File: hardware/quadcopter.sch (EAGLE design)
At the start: 66 parts, among them J1 AVR_SPI_PRG_6NS, J2 HEADER-4POS-2X2-0.1IN-FEMALE-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, J3 HEADER-10POSTH-254X10, J4 HEADER-4POS-2X2-0.1IN-FEMALE-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, Q3 MOSFET-FET-SI2302CDS-T1-E3CT-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, Q4 MOSFET-FET-SI2302CDS-T1-E3CT-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, Q5 MOSFET-FET-SI2302CDS-T1-E3CT-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, Q6 MOSFET-FET-SI2302CDS-T1-E3CT-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, U1 ATMEGA128RFA1, U2 IMU-LSM6DSOXTR-497-18367-1-ND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, Y1 CRYSTAL5X3

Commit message: please work
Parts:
- removed D10, D3, D4, D9: (no value), custom_v9:LED-RED-160-1178-1-ND
- added U$1, U$4, U$5, U$6: LED_BLUE, LED:LED_BLUE
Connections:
- removed net N$12: C9.2, U2.VDD
- net 3V: now also C9.2, U2.VDD
- net LED1: no longer D3.A
- net LED2: no longer D4.A
- net LED3: no longer D9.A
- net LED4: no longer D10.A
- net N$22: no longer D10.C, D3.C, D4.C, D9.C
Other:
- moved on the sheet: R6
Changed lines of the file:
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@@
 <part name="J3" library="quadparts_prebuilt_2022" deviceset="HEADER-10POS" device="TH-254X10"/>
 <part name="J4" library="quadparts_prebuilt_2022" deviceset="HEADER-4POS" device="-2X2-0.1IN-FEMALE-SMD-BOTTOM-ENTRY"/>
-<part name="D3" library="custom_v9" deviceset="LED" device="-RED-160-1178-1-ND"/>
-<part name="D4" library="custom_v9" deviceset="LED" device="-RED-160-1178-1-ND"/>
-<part name="D9" library="custom_v9" deviceset="LED" device="-RED-160-1178-1-ND"/>
-<part name="D10" library="custom_v9" deviceset="LED" device="-RED-160-1178-1-ND"/>
 <part name="GND23" library="quadparts_prebuilt_2022" deviceset="GND" device=""/>
 <part name="R6" library="quadparts_prebuilt_2022" deviceset="RESISTOR_" device="SMD-2012-0805-604" value="604"/>
@@
 <part name="GND43" library="quadparts_prebuilt_2022" deviceset="GND" device=""/>
 <part name="P+19" library="quadparts_prebuilt_2022" deviceset="3V" device=""/>
+<part name="U$1" library="LED" library_urn="urn:adsk.wipprod:fs.file:vf.dgQ34RYLRkWtLog4lTO-XQ" deviceset="LED_BLUE" device=""/>
+<part name="U$4" library="LED" library_urn="urn:adsk.wipprod:fs.file:vf.dgQ34RYLRkWtLog4lTO-XQ" deviceset="LED_BLUE" device=""/>
+<part name="U$5" library="LED" library_urn="urn:adsk.wipprod:fs.file:vf.dgQ34RYLRkWtLog4lTO-XQ" deviceset="LED_BLUE" device=""/>
+<part name="U$6" library="LED" library_urn="urn:adsk.wipprod:fs.file:vf.dgQ34RYLRkWtLog4lTO-XQ" deviceset="LED_BLUE" device=""/>
 </parts>
 <sheets>
@@
 <attribute name="NAME" x="155.702" y="55.88" size="1.778" layer="95" rot="R180"/>
 </instance>
-<instance part="D3" gate="G$1" x="91.44" y="7.62" smashed="yes">
-<attribute name="NAME" x="86.36" y="10.16" size="1.778" layer="95"/>
-<attribute name="VALUE" x="86.36" y="2.54" size="1.778" layer="96"/>
-</instance>
-<instance part="D4" gate="G$1" x="91.44" y="0" smashed="yes">
-<attribute name="NAME" x="86.36" y="2.54" size="1.778" layer="95"/>
-<attribute name="VALUE" x="86.36" y="-5.08" size="1.778" layer="96"/>
-</instance>
-<instance part="D9" gate="G$1" x="91.44" y="-7.62" smashed="yes">
-<attribute name="NAME" x="86.36" y="-5.08" size="1.778" layer="95"/>
-<attribute name="VALUE" x="86.36" y="-12.7" size="1.778" layer="96"/>
-</instance>
-<instance part="D10" gate="G$1" x="91.44" y="-15.24" smashed="yes">
-<attribute name="NAME" x="86.36" y="-12.7" size="1.778" layer="95"/>
-<attribute name="VALUE" x="86.36" y="-20.32" size="1.778" layer="96"/>
-</instance>
-<instance part="GND23" gate="1" x="96.52" y="-43.18" smashed="yes">
-<attribute name="VALUE" x="96.52" y="-45.72" size="1.778" layer="96" align="center"/>
-</instance>
-<instance part="R6" gate="G$1" x="96.52" y="-27.94" smashed="yes" rot="R90">
-<attribute name="VALUE" x="99.822" y="-31.75" size="1.778" layer="96" rot="R90"/>
-<attribute name="NAME" x="95.0214" y="-31.75" size="1.778" layer="95" rot="R90"/>
+<instance part="GND23" gate="1" x="104.14" y="-43.18" smashed="yes">
+<attribute name="VALUE" x="104.14" y="-45.72" size="1.778" layer="96" align="center"/>
+</instance>
+<instance part="R6" gate="G$1" x="104.14" y="-27.94" smashed="yes" rot="R90">
+<attribute name="VALUE" x="107.442" y="-31.75" size="1.778" layer="96" rot="R90"/>
+<attribute name="NAME" x="102.6414" y="-31.75" size="1.778" layer="95" rot="R90"/>
 </instance>
 <instance part="GND37" gate="1" x="121.92" y="-43.18" smashed="yes">
@@
 <attribute name="VALUE" x="83.82" y="-91.44" size="1.778" layer="96" rot="R180" align="center"/>
 </instance>
+<instance part="U$1" gate="G$1" x="93.98" y="0" smashed="yes"/>
+<instance part="U$4" gate="G$1" x="93.98" y="7.62" smashed="yes"/>
+<instance part="U$5" gate="G$1" x="93.98" y="-15.24" smashed="yes"/>
+<instance part="U$6" gate="G$1" x="93.98" y="-7.62" smashed="yes"/>
 </instances>
 <busses>
@@
 </segment>
 <segment>
-<wire x1="96.52" y1="-33.02" x2="96.52" y2="-40.64" width="0.1524" layer="91"/>
+<wire x1="104.14" y1="-33.02" x2="104.14" y2="-40.64" width="0.1524" layer="91"/>
 <pinref part="GND23" gate="1" pin="GND"/>
 <pinref part="R6" gate="G$1" pin="1"/>
@@
 <junction x="68.58" y="-101.6"/>
 </segment>
+<segment>
+<pinref part="P+6" gate="G$1" pin="3V"/>
+<wire x1="119.38" y1="134.62" x2="119.38" y2="127" width="0.1524" layer="91"/>
+<pinref part="U2" gate="G$1" pin="VDD"/>
+<wire x1="124.46" y1="127" x2="119.38" y2="127" width="0.1524" layer="91"/>
+<pinref part="C9" gate="G$1" pin="2"/>
+<junction x="119.38" y="127"/>
+</segment>
 </net>
 <net name="SCK" class="0">
@@
 </segment>
 <segment>
-<pinref part="D4" gate="G$1" pin="A"/>
 <wire x1="86.36" y1="0" x2="81.28" y2="0" width="0.1524" layer="91"/>
 <label x="81.28" y="0" size="1.778" layer="95" rot="R180" xref="yes"/>
@@
 </segment>
 <segment>
-<pinref part="D9" gate="G$1" pin="A"/>
 <wire x1="86.36" y1="-7.62" x2="81.28" y2="-7.62" width="0.1524" layer="91"/>
 <label x="81.28" y="-7.62" size="1.778" layer="95" rot="R180" xref="yes"/>
@@
 </segment>
 <segment>
-<pinref part="D10" gate="G$1" pin="A"/>
 <wire x1="86.36" y1="-15.24" x2="81.28" y2="-15.24" width="0.1524" layer="91"/>
 <label x="81.28" y="-15.24" size="1.778" layer="95" rot="R180" xref="yes"/>
@@
 <pinref part="J2" gate="G$1" pin="1"/>
 <pinref part="C13" gate="G$1" pin="2"/>
-</segment>
-</net>
-<net name="N$12" class="0">
-<segment>
-<pinref part="U2" gate="G$1" pin="VDD"/>
-<wire x1="124.46" y1="127" x2="119.38" y2="127" width="0.1524" layer="91"/>
-<wire x1="119.38" y1="134.62" x2="119.38" y2="127" width="0.1524" layer="91"/>
-<pinref part="P+6" gate="G$1" pin="3V"/>
-<pinref part="C9" gate="G$1" pin="2"/>
-<junction x="119.38" y="127"/>
 </segment>
 </net>
@@
 </segment>
 <segment>
-<pinref part="D3" gate="G$1" pin="A"/>
 <wire x1="86.36" y1="7.62" x2="81.28" y2="7.62" width="0.1524" layer="91"/>
 <label x="81.28" y="7.62" size="1.778" layer="95" rot="R180" xref="yes"/>
@@
 <net name="N$22" class="0">
 <segment>
-<pinref part="D3" gate="G$1" pin="C"/>
-<pinref part="D4" gate="G$1" pin="C"/>
-<wire x1="96.52" y1="-15.24" x2="96.52" y2="-7.62" width="0.1524" layer="91"/>
-<wire x1="96.52" y1="-7.62" x2="96.52" y2="0" width="0.1524" layer="91"/>
-<wire x1="96.52" y1="0" x2="96.52" y2="7.62" width="0.1524" layer="91"/>
-<pinref part="D9" gate="G$1" pin="C"/>
-<pinref part="D10" gate="G$1" pin="C"/>
-<junction x="96.52" y="0"/>
-<junction x="96.52" y="-7.62"/>
-<wire x1="96.52" y1="-15.24" x2="96.52" y2="-22.86" width="0.1524" layer="91"/>
-<junction x="96.52" y="-15.24"/>
+<wire x1="104.14" y1="-15.24" x2="104.14" y2="-7.62" width="0.1524" layer="91"/>
+<wire x1="104.14" y1="-7.62" x2="104.14" y2="0" width="0.1524" layer="91"/>
+<wire x1="104.14" y1="0" x2="104.14" y2="7.62" width="0.1524" layer="91"/>
+<wire x1="104.14" y1="-15.24" x2="104.14" y2="-22.86" width="0.1524" layer="91"/>
 <pinref part="R6" gate="G$1" pin="2"/>
 </segment>
@@
 </drawing>
 <compatibility>
+<note version="8.2" severity="warning">
+Since Version 8.2, EAGLE supports online libraries. The ids
+of those online libraries will not be understood (or retained)
+with this version.
+</note>
 <note version="8.3" severity="warning">
 Since Version 8.3, EAGLE supports URNs for individual library

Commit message: fixed power supply stuff, a lot of broken led nets, still havent found N...
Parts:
- removed B2: BATTERY-SCREW-TERMINAL-MINI-SMD, quadparts_prebuilt_2022:BATTERY-SCREW-TERMINAL-MINI-SMD
- removed C14, C15: 1uF, quadparts_prebuilt_2022:CAPACITOR-NP_SMD-2012-0805_CERAMIC-1UF
- removed C16: 47uF, quadparts_prebuilt_2022:CAPACITOR-POL_47UF-SMD-1206-TAJA
- removed S1: POWER-SWITCH-MFS201N-9-Z-SMD-EDGE, quadparts_prebuilt_2022:POWER-SWITCH-MFS201N-9-Z-SMD-EDGE
- removed U$1, U$4, U$5, U$6: LED_BLUE, LED:LED_BLUE
- removed VOLTAGE_REGULATOR: 3V, quadparts_prebuilt_2022:TPS73633-DBVT3V
- added LED1, LED2, LED3, LED4: LED_YELLOW, LED:LED_YELLOW
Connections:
- removed net N$17: C15.2, VOLTAGE_REGULATOR.EN
- removed net N$22: R6.2
- removed net N$23: B2.N, S1.C
- new net N$12: LED1.C, LED2.C, LED3.C, LED4.C, R6.2
- net 3V: now also C10.1, U2.VDDIO; no longer C14.1, C16.+, VOLTAGE_REGULATOR.OUT
- net BAT_GND: no longer S1.OFF, VOLTAGE_REGULATOR.GND
- net GND: no longer C14.2, C16.-
- net LED1: now also LED1.A
- net LED2: now also LED2.A
- net LED3: now also LED3.A
- net LED4: now also LED4.A
- net N$13: now also C12.1, J1.5; no longer C10.1, U2.VDDIO
- net RESET: no longer C12.1, J1.5
- net VBAT: no longer B2.P, C15.1, S1.ON, VOLTAGE_REGULATOR.IN
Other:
- note added: "Debug/Rescue Header"
- note added: "IMU"
- note added: "LED"
- note added: "Motor Driver"
- note added: "Voltage Calculations LED: 3v source, 604 ohms, 2v voltage drop results in 1.66 mA through LED, well below limit of 100 mA. Also within microcontroller capability"
- note added: "Voltage Regulator"
- moved on the sheet: B4, C12, C17, C18, C19, D2, R2, S2, VOLTAGE_REGULATOR1

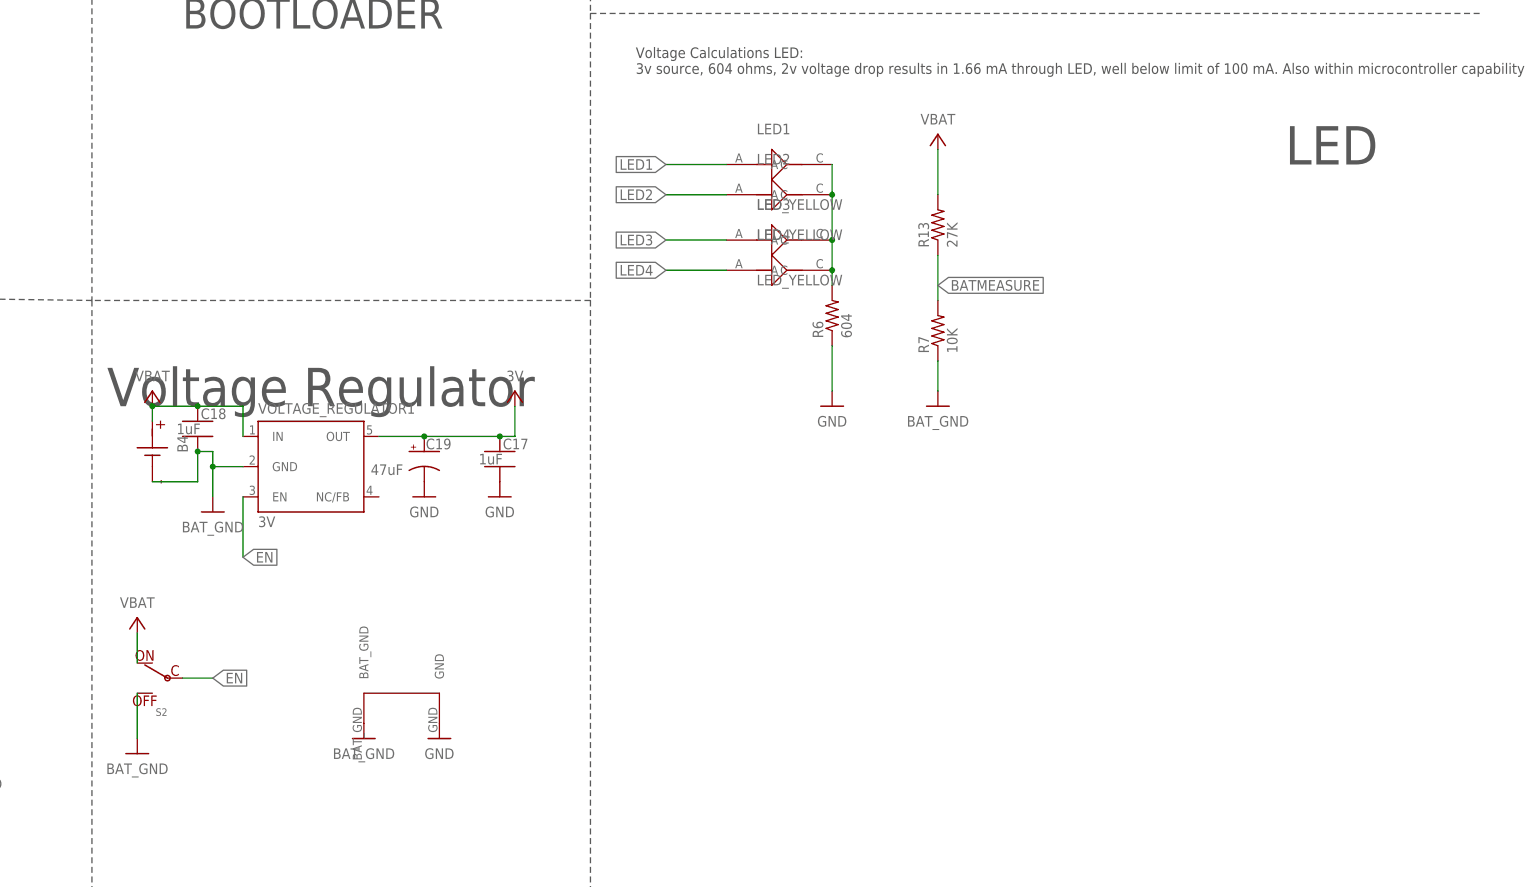
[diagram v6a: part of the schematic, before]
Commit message: fixing library issues mostly, also a netbrige error, stil cant find N
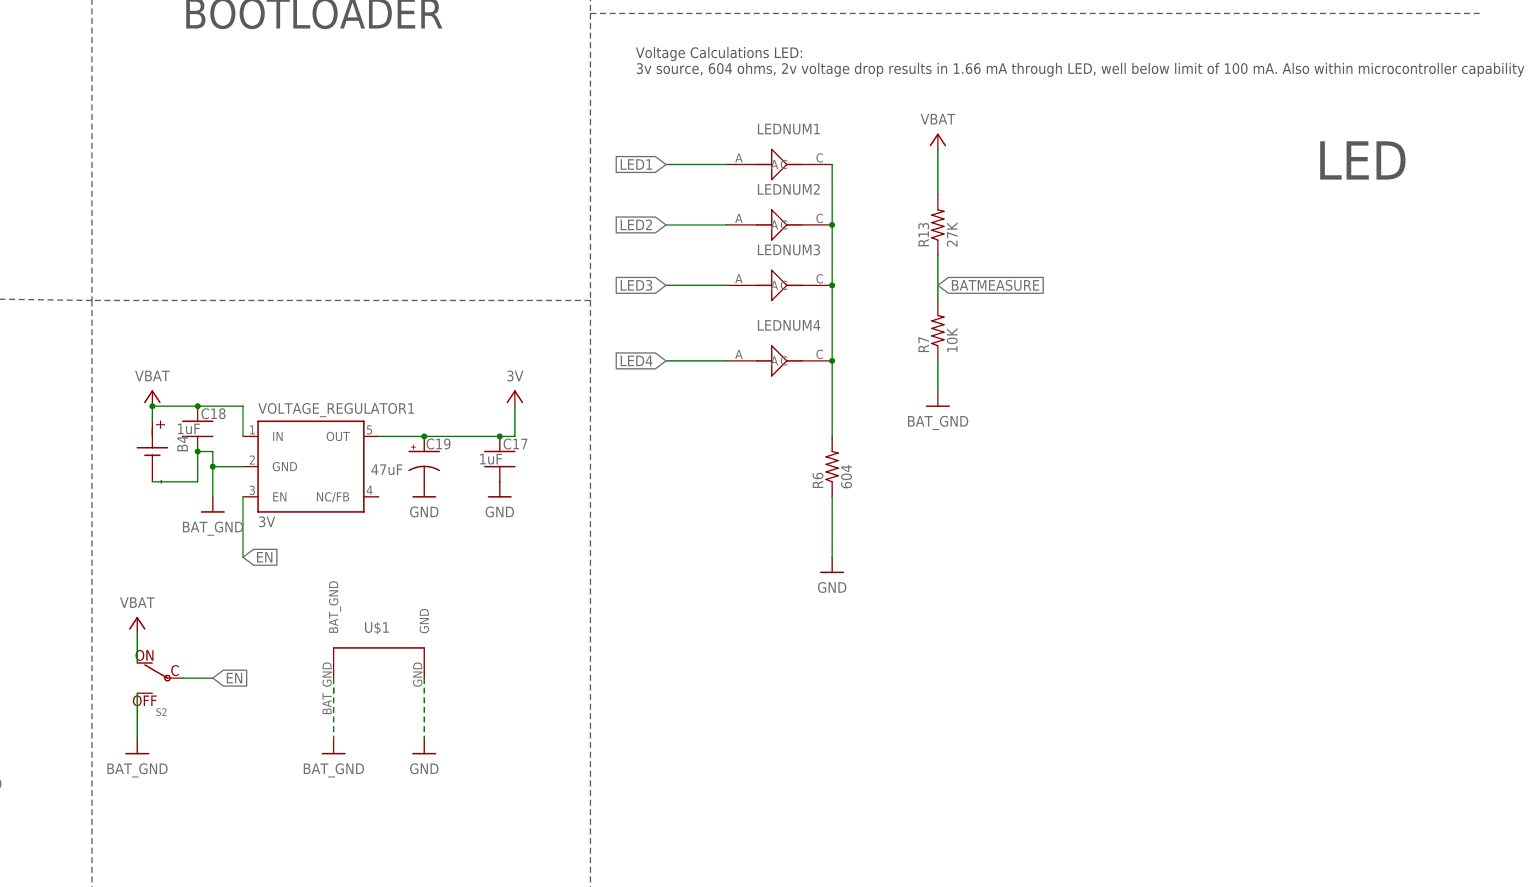
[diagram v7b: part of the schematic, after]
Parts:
- removed LED2, LED3, LED4: LED_YELLOW, LED:LED_YELLOW
- removed U$2: NETBRIDGE, custom:NETBRIDGE
- added LEDNUM2, LEDNUM3, LEDNUM4: LED_YELLOW, LED:LED_YELLOW
- added U$1: NETBRIDGE, custom_v9:NETBRIDGE
- renumbered LED1 to LEDNUM1
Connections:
- net BAT_GND: now also U$1.BAT_GND; no longer U$2.BAT_GND
- net GND: now also U$1.GND; no longer U$2.GND
- net LED2: now also LEDNUM2.A; no longer LED2.A
- net LED3: now also LEDNUM3.A; no longer LED3.A
- net LED4: now also LEDNUM4.A; no longer LED4.A
- net N$12: now also LEDNUM2.C, LEDNUM3.C, LEDNUM4.C; no longer LED2.C, LED3.C, LED4.C
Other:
- note removed: "Voltage Regulator"
- moved on the sheet: R6
